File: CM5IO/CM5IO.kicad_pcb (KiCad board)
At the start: 4 copper layers, 59.7 x 78 mm, 65 parts, among them J1 POWER TERMINAL, J11 USB_C_Receptacle_USB2.0, J12 USB3_A, J14 JST_SHBM04B-SRSS-TB, J16 Conn_01x22_Female, J2 Conn_02x06_Odd_Even, J22 46765-1301, J3 62674-161121ALF, J4 J_PSU_EN, J5 Conn_01x22_Female, J7 Micro_SD_Card_Det, J8 THD-20-R, SW1 Right angle Tact button, U12 RT9742SNGV, U18 RT9742GGJ5, U6 AP22653W6

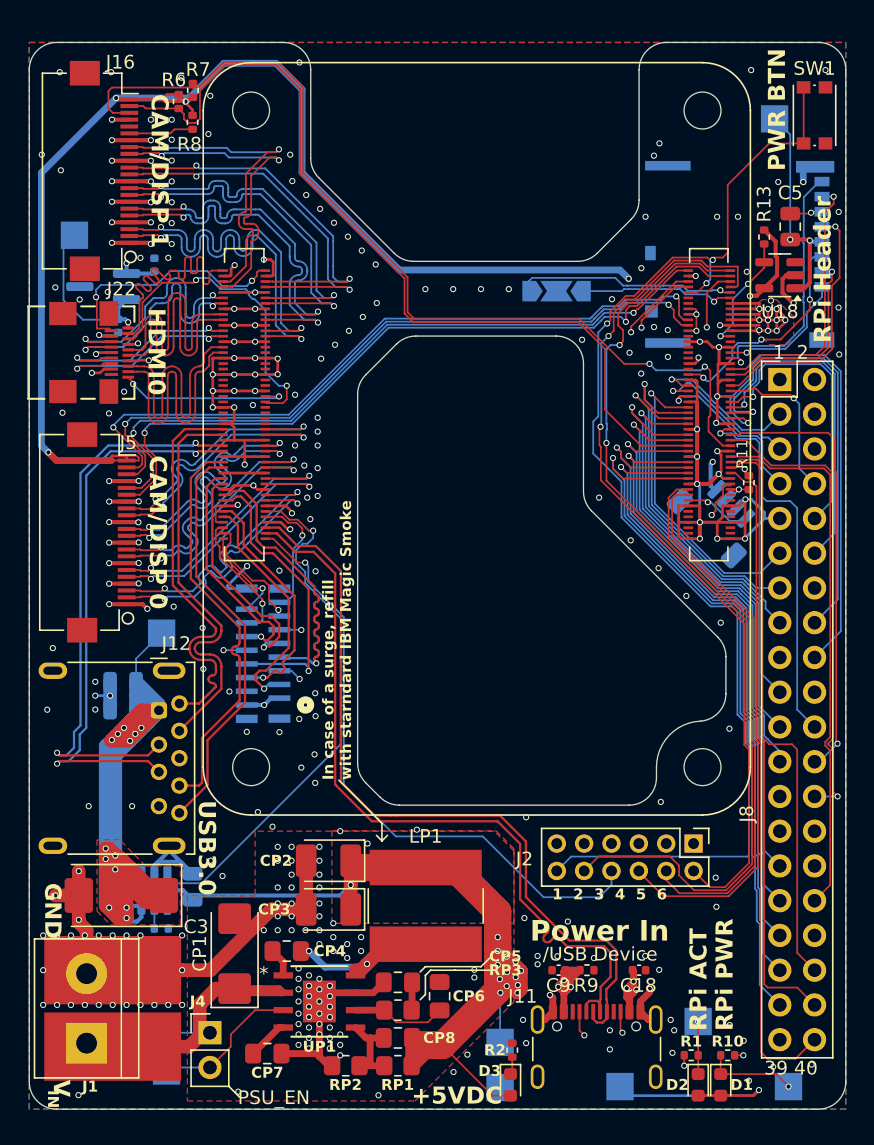
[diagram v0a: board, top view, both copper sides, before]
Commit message: change LEDs orientation
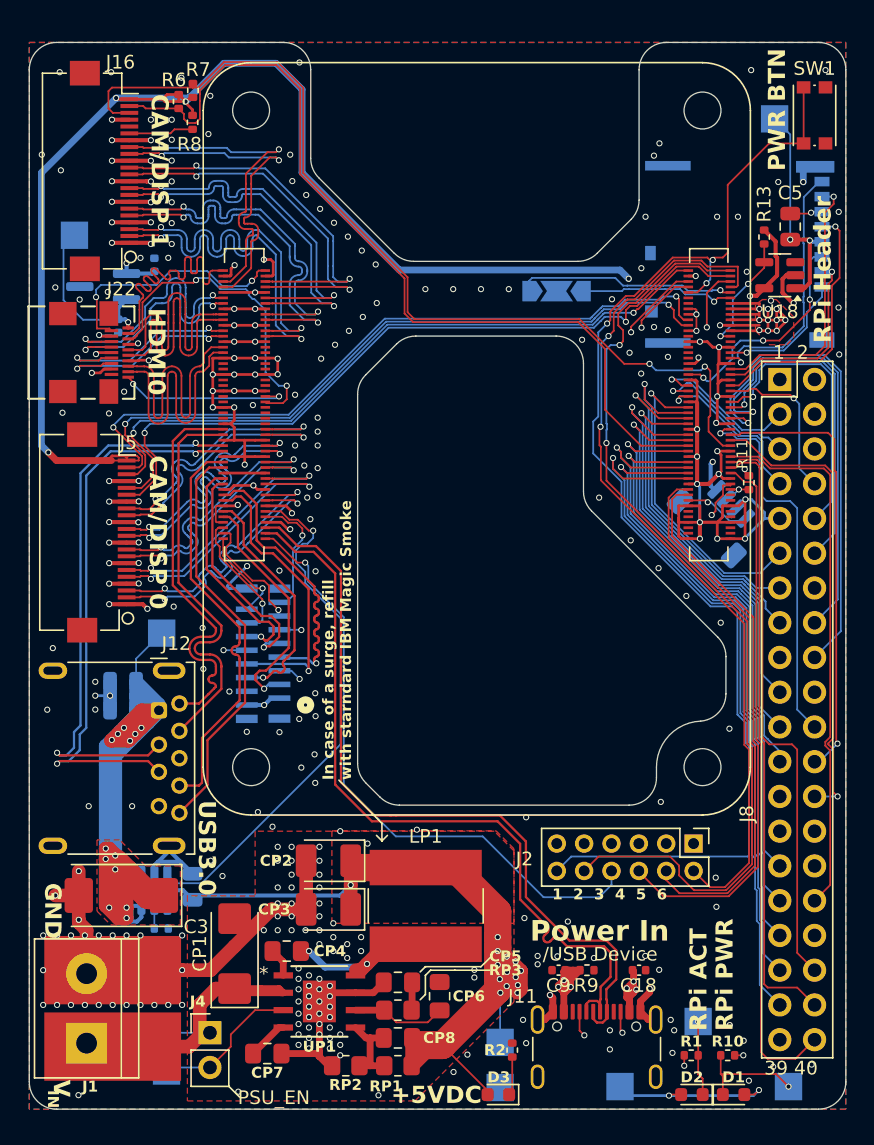
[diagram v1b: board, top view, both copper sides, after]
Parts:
- moved D1 1.18 mm to (197.8, 145.4), turned to 0 degrees
- moved D3 1.14 mm to (180.6, 145.4), turned to 180 degrees
- moved D2 0.85 mm to (194.7, 145.4), turned to 180 degrees
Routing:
- net /+3.3v: track 200.8 -> 198.3 mm, vias 9 -> 10
- net Net-(D2-K): track 3.85 -> 5.48 mm
- net Net-(D1-K): track 6.70 -> 8.27 mm
- net /+5v: track 327.1 -> 325.6 mm
- net Net-(D3-K): track 1.30 -> 2.69 mm
